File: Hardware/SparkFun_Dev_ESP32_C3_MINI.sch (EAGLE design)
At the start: 41 parts, among them J1 USB Female Type C Connector, J5 Vertical Qwiic Connector, U1 ESP32-C3_MINI-1, U2 RT9080-33GJ5

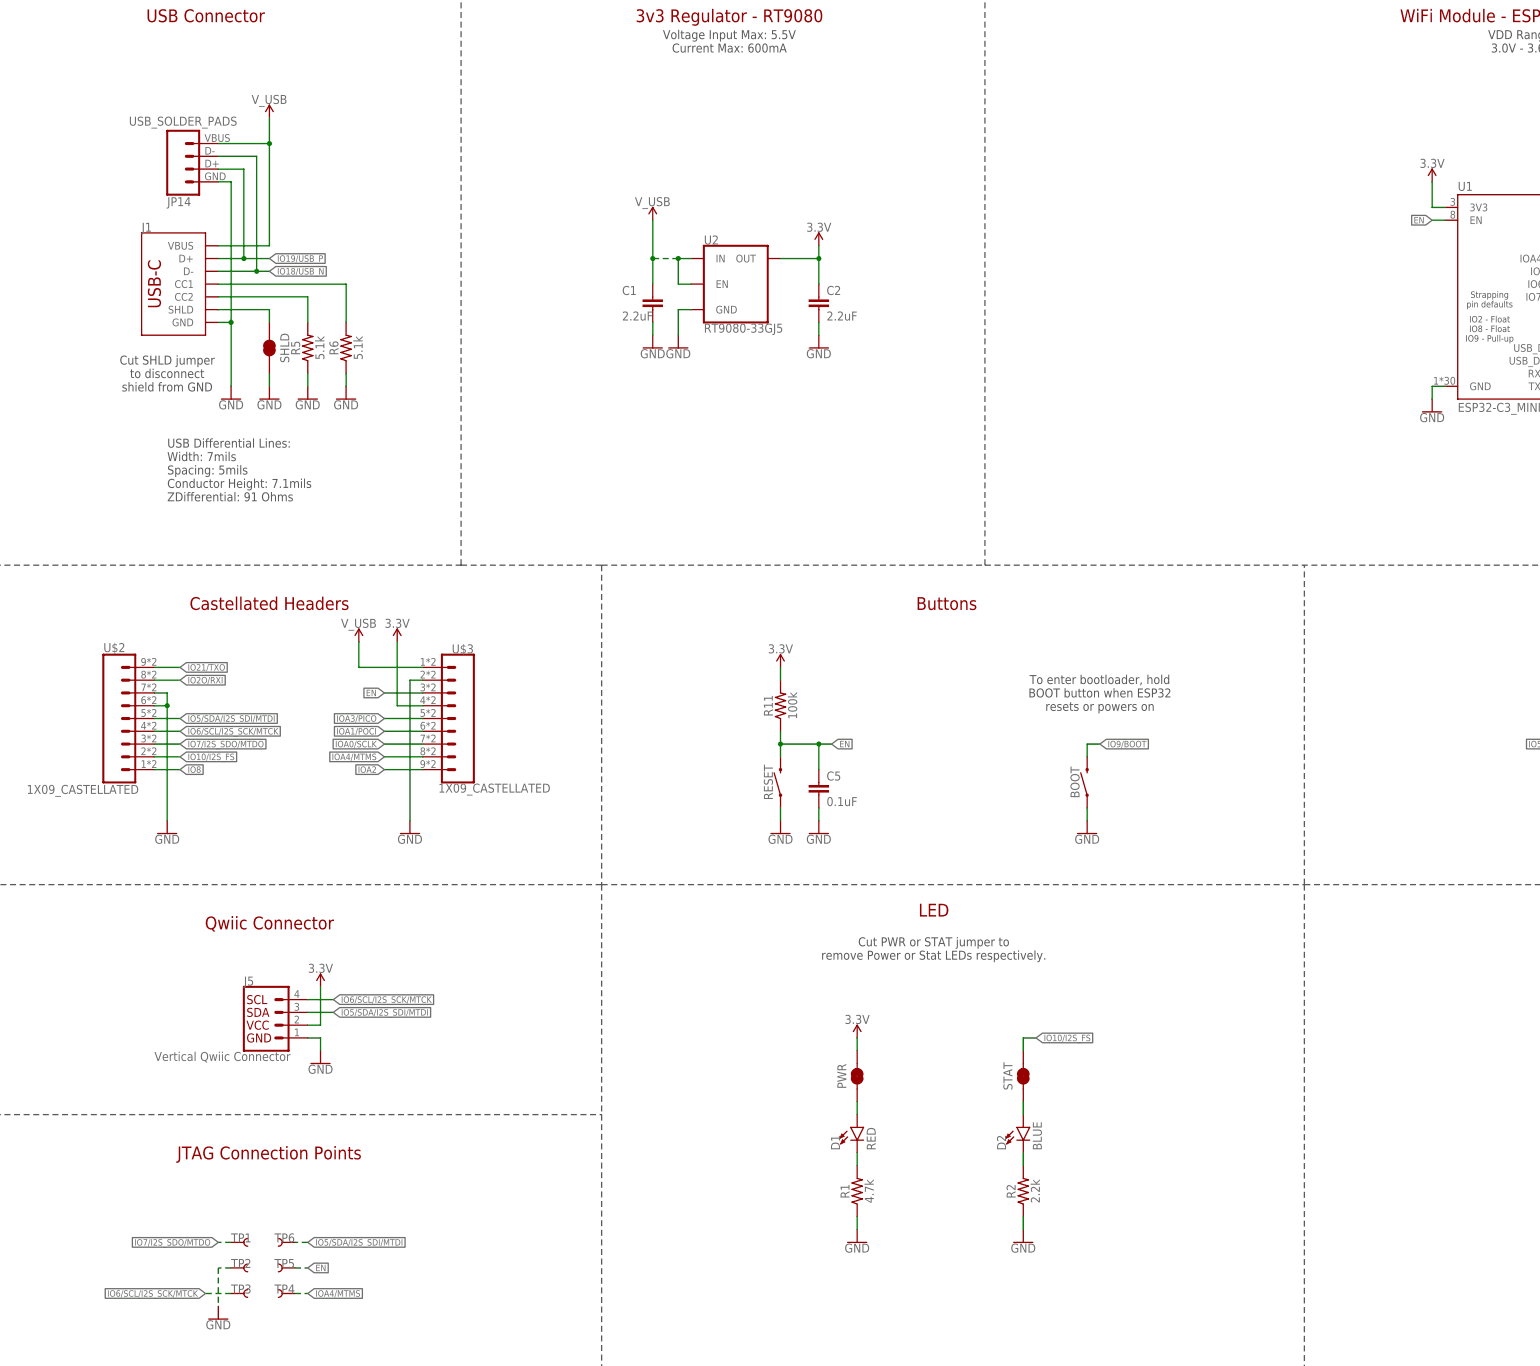
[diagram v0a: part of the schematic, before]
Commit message: Shortens some nets, fixes some silk
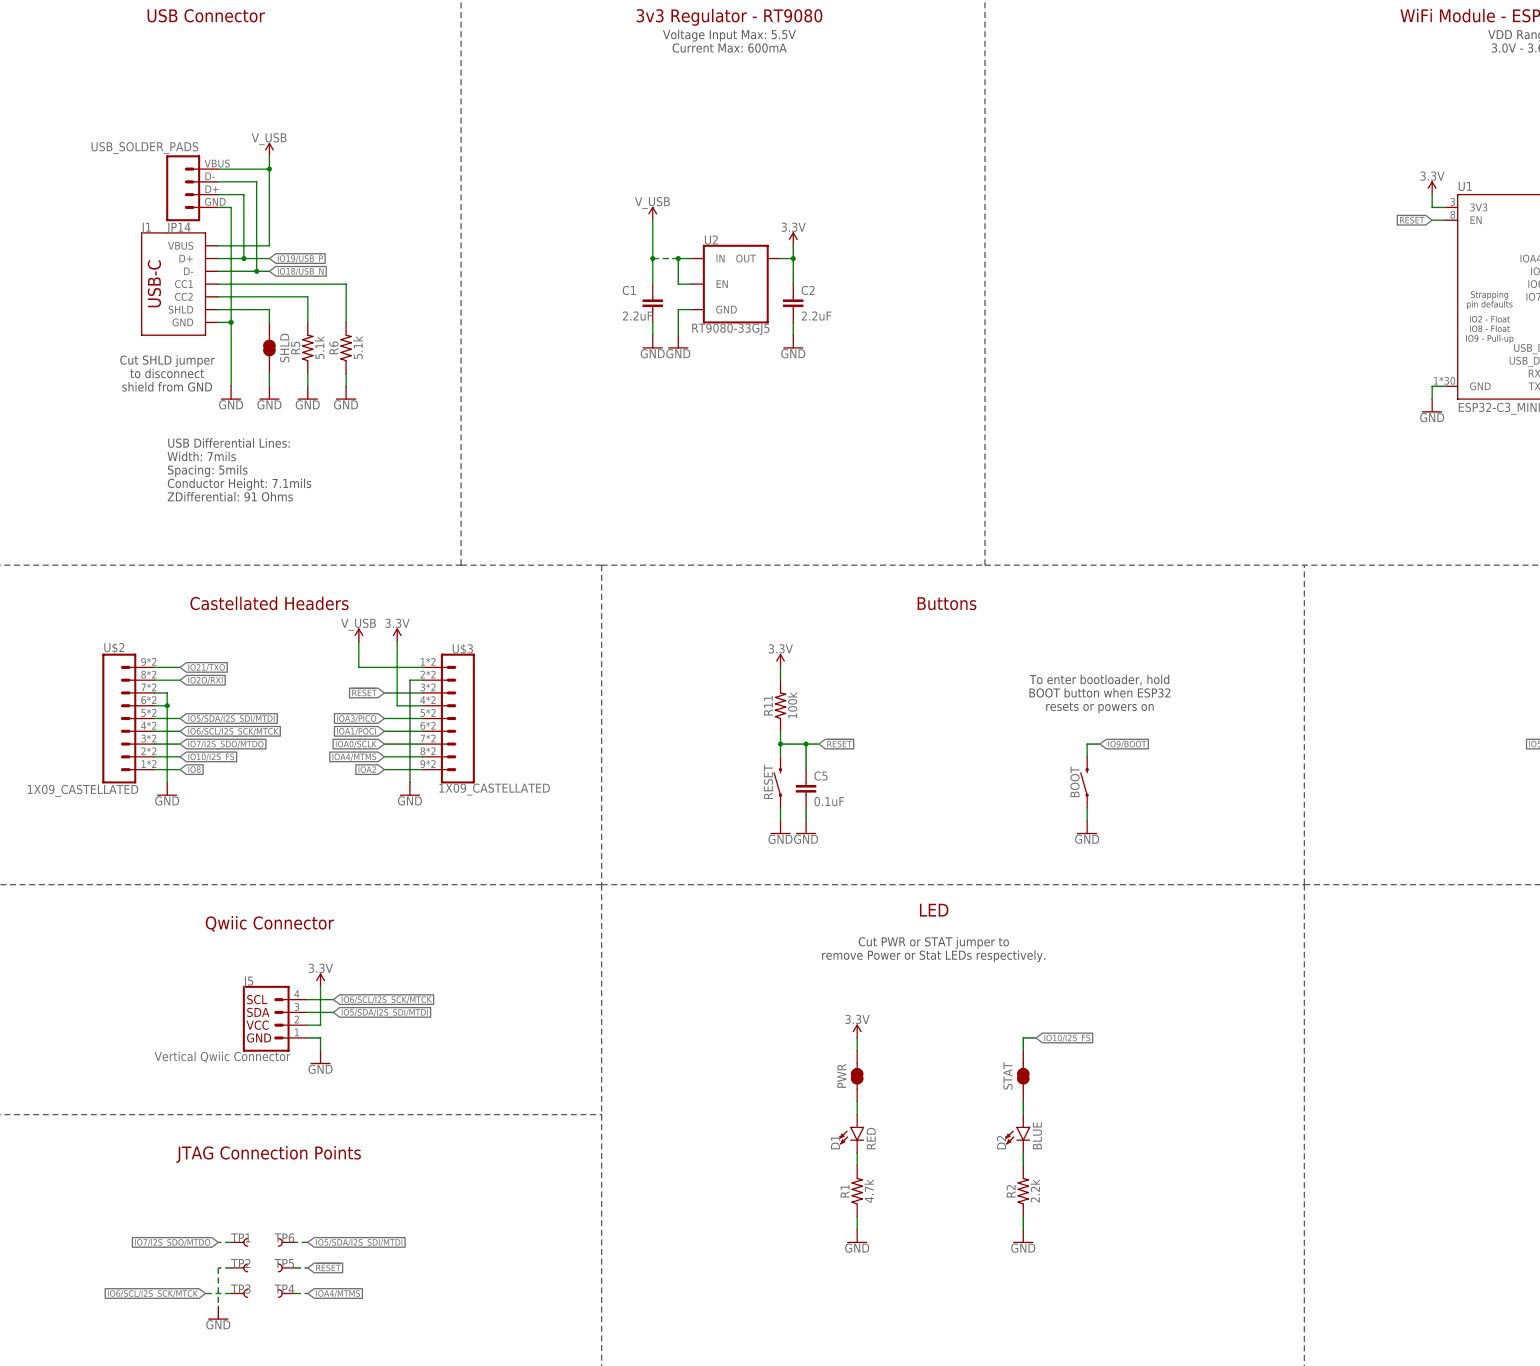
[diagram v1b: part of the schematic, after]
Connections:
- net EN renamed !RESET!
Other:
- moved on the sheet: C2, C5, JP14

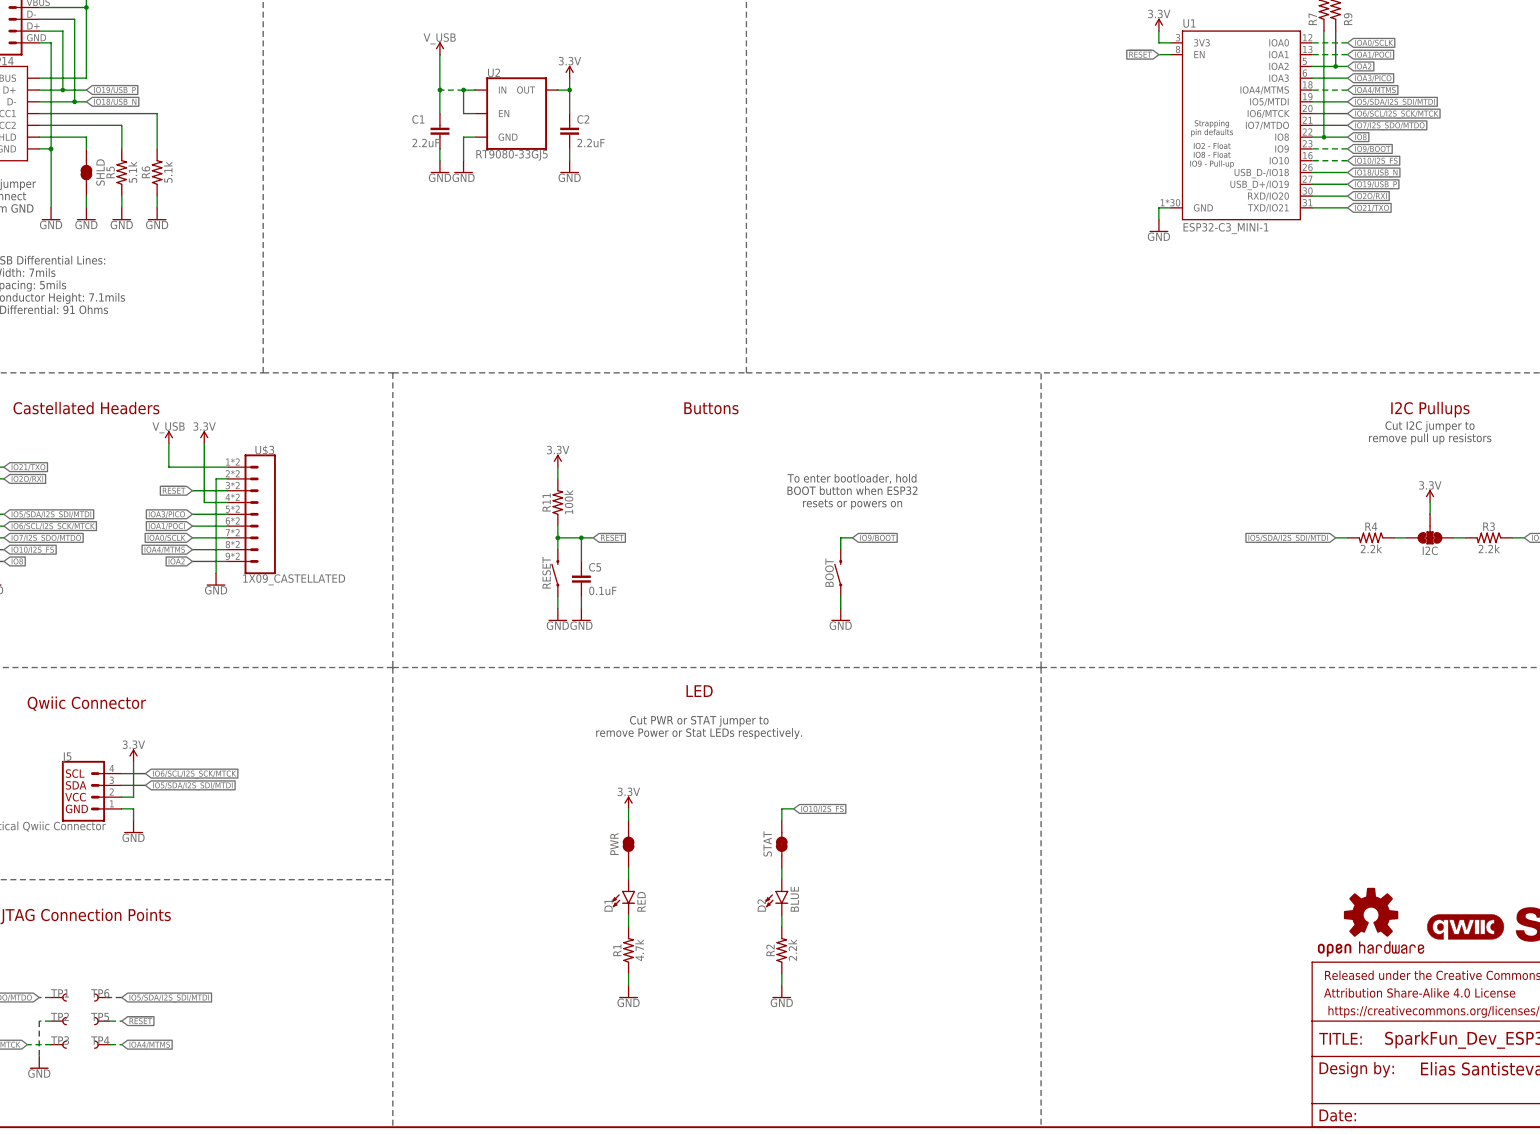
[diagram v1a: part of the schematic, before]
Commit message: Renames I2S pins
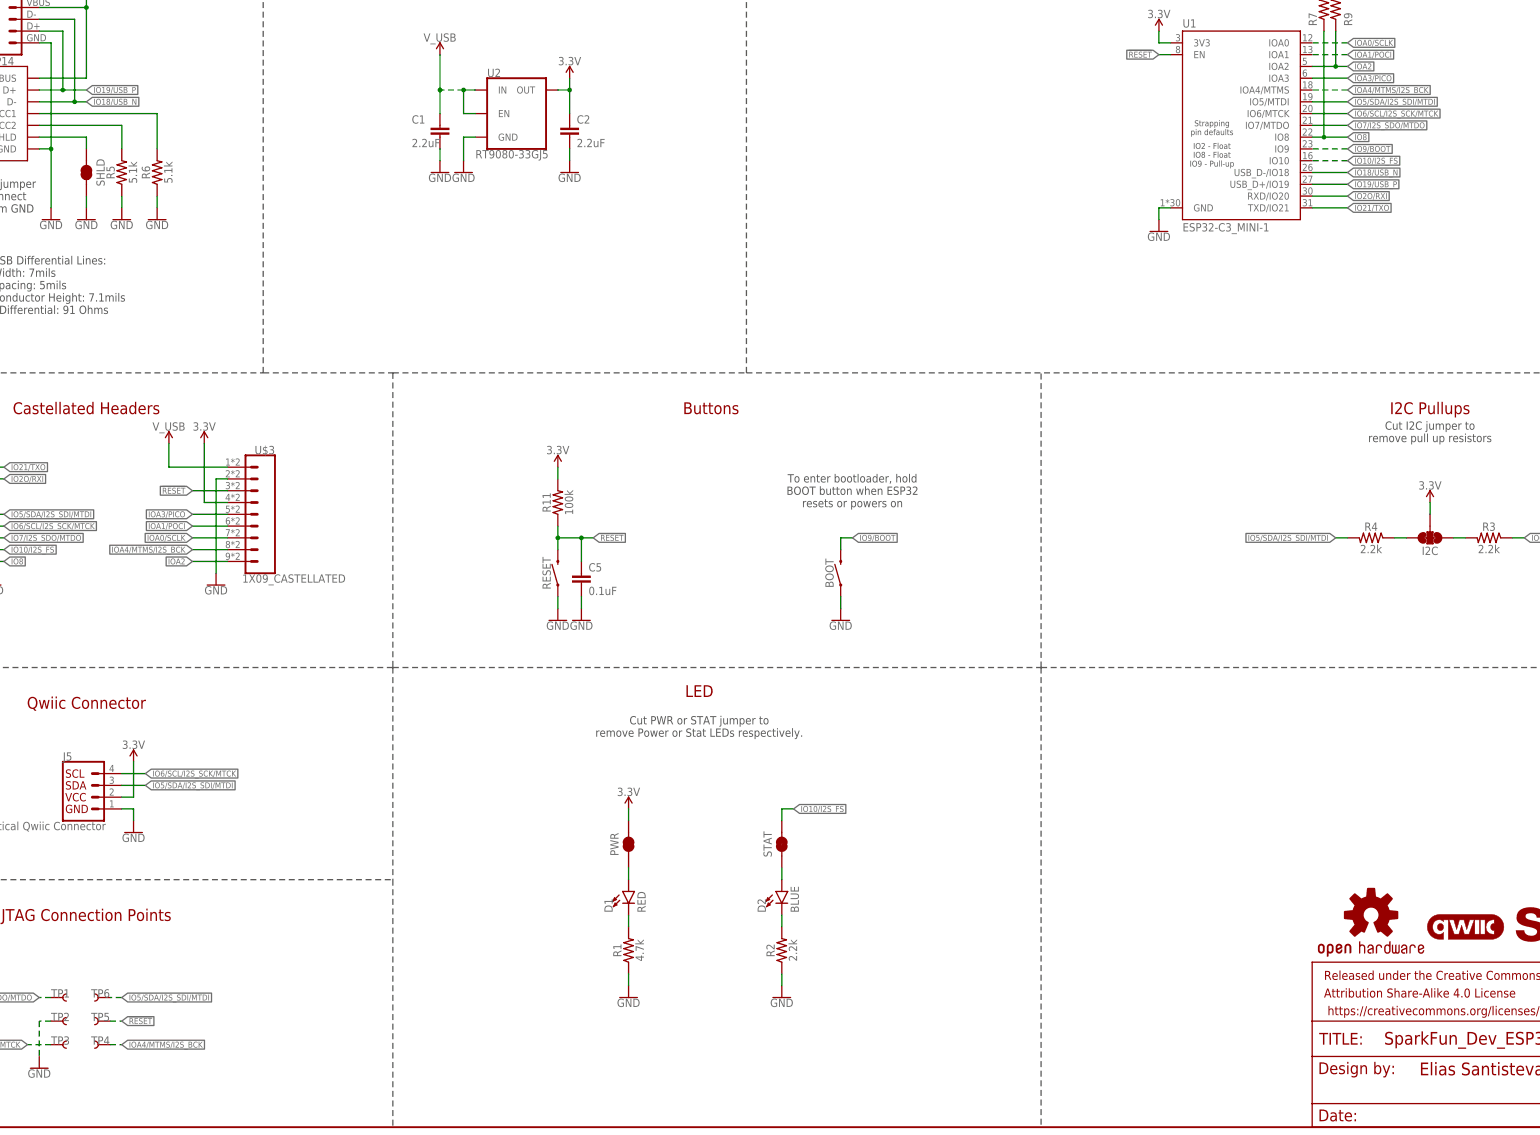
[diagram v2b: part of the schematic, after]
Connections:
- net IOA4/MTMS renamed IOA4/MTMS/I2S_BCK
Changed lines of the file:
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@@
 </segment>
 </net>
-<net name="IOA4/MTMS" class="0">
+<net name="IOA4/MTMS/I2S_BCK" class="0">
 <segment>
 <wire x1="685.8" y1="223.52" x2="678.18" y2="223.52" width="0.1524" layer="91" style="longdash"/>

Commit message: Adds numerous aesthetic changes
* Increases size of silk everywhere possible
* Moves jumpers for LEDs to the corners underneath the respective LED.
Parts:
- D1: value RED -> Red
- D2: value BLUE -> Blue
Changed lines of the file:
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@@
 <part name="SUPPLY2" library="SparkFun-PowerSymbols" deviceset="3.3V" device=""/>
 <part name="GND4" library="SparkFun-PowerSymbols" deviceset="GND" device=""/>
-<part name="D1" library="SparkFun-LED" deviceset="LED-RED" device="_0603-KB" value="RED"/>
+<part name="D1" library="SparkFun-LED" deviceset="LED-RED" device="_0603-KB" value="Red"/>
 <part name="R1" library="SparkFun-Resistors" deviceset="4.7KOHM" device="-0402T-1/16W-1%" value="4.7k"/>
 <part name="PWR" library="SparkFun-Jumpers" deviceset="JUMPER-SMT_2_NC_TRACE" device="_SILK" package3d_urn="urn:adsk.eagle:package:39281/1"/>
@@
 <attribute name="REV" value="v01"/>
 </part>
-<part name="D2" library="SparkFun-LED" deviceset="LED-BLUE" device="0603" value="BLUE"/>
+<part name="D2" library="SparkFun-LED" deviceset="LED-BLUE" device="0603" value="Blue"/>
 <part name="R2" library="SparkFun-Resistors" deviceset="2.2KOHM" device="-0402T-1/16W-1%" value="2.2k"/>
 <part name="STAT" library="SparkFun-Jumpers" deviceset="JUMPER-SMT_2_NC_TRACE" device="_SILK" package3d_urn="urn:adsk.eagle:package:39281/1"/>

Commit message: Adds more aesthetic changes
* Note on previous commit: I2C labels were removed from silk
* Fixes ground silk rectangle
* rotates qwiic label
* Shrinks VBUS polygon
* Moves boot capacitor to other side of button
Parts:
- removed LOGO2: QWIIC_LOGO_3MM, SparkFun-Aesthetics:QWIIC_LOGO_3MM
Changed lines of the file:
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@@
 <part name="FD3" library="SparkFun-Aesthetics" deviceset="FIDUCIAL" device="UFIDUCIAL"/>
 <part name="FD4" library="SparkFun-Aesthetics" deviceset="FIDUCIAL" device="UFIDUCIAL"/>
-<part name="LOGO2" library="SparkFun-Aesthetics" deviceset="QWIIC_LOGO" device="_3MM"/>
 <part name="LOGO3" library="SparkFun-Aesthetics" deviceset="OSHW-LOGO" device="S"/>
 <part name="R7" library="SparkFun-Resistors" deviceset="100KOHM" device="-0402T-1/16W-1%" value="100k"/>
@@
 <instance part="FD3" gate="G$1" x="767.08" y="30.48" smashed="yes"/>
 <instance part="FD4" gate="G$1" x="769.62" y="30.48" smashed="yes"/>
-<instance part="LOGO2" gate="G$1" x="711.2" y="43.18" smashed="yes"/>
 <instance part="LOGO3" gate="G$1" x="690.88" y="45.72" smashed="yes"/>
 <instance part="R7" gate="G$1" x="680.72" y="241.3" smashed="yes" rot="R90">
